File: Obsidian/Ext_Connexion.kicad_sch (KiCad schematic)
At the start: 35 parts, among them J4 Conn_02x20_Odd_Even

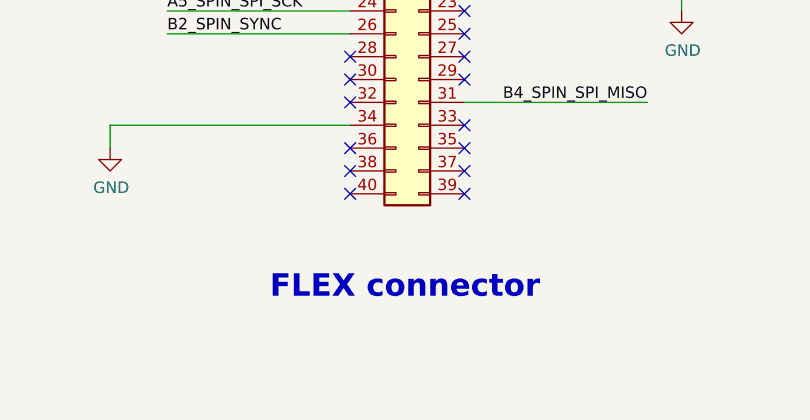
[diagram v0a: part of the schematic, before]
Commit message: Changed the layout so that we have guard rails. Changed USB and RJ45 position Changed Flex connector position. Changed flash LDO position Improved silkscreen. Changed outline around RJ45. Changed SFP cage footprint. Added a rule for Earth clearance.
Signed-off-by: Jean Alinei <jean.alinei@owntech.org>
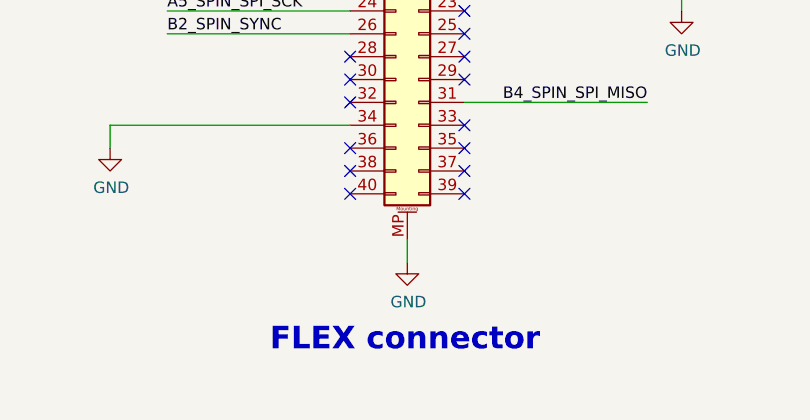
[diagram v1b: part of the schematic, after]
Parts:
- J4: symbol Connector_Generic:Conn_02x20_Odd_Even -> Connector_Generic_MountingPin:Conn_02x20_Odd_Even_MountingPin
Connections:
- net GND: now also J4.MP (MountPin)
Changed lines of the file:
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@@
 	(text "FLEX connector\n"
 		(exclude_from_sim no)
-		(at 64.516 184.404 0)
+		(at 64.516 190.246 0)
 		(effects
 			(font
@@
 	(wire
 		(pts
+			(xy 64.77 179.07) (xy 64.77 181.61)
+		)
+		(stroke
+			(width 0)
+			(type default)
+		)
+	)
+	(wire
+		(pts
 			(xy 101.6 72.39) (xy 101.6 71.12)
 		)
@@
 	)
 	(symbol
+		(lib_id "Library_Symbol:GND")
+		(at 64.77 181.61 0)
+		(unit 1)
+		(exclude_from_sim no)
+		(in_bom yes)
+		(on_board yes)
+		(dnp no)
+		(property "Reference" "#PWR0295"
+			(at 64.77 187.96 0)
+			(effects
+				(font
+					(size 1.27 1.27)
+				)
+				(hide yes)
+			)
+		)
+		(property "Value" "GND"
+			(at 64.897 186.0042 0)
+			(effects
+				(font
+					(size 1.27 1.27)
+				)
+			)
+		)
+		(property "Footprint" ""
+			(at 64.77 181.61 0)
+			(effects
+				(font
+					(size 1.27 1.27)
+				)
+				(hide yes)
+			)
+		)
+		(property "Datasheet" ""
+			(at 64.77 181.61 0)
+			(effects
+				(font
+					(size 1.27 1.27)
+				)
+				(hide yes)
+			)
+		)
+		(property "Description" ""
+			(at 64.77 181.61 0)
+			(effects
+				(font
+					(size 1.27 1.27)
+				)
+				(hide yes)
+			)
+		)
+		(pin "1"
+		)
+		(instances
+			(project "Obsidian"
+				(path "/c2a4f786-b14c-434a-acf7-b20fb2221b0b/37c76a7d-e360-409e-9f8e-819f870af943"
+					(reference "#PWR0295")
+					(unit 1)
+				)
+			)
+		)
+	)
+	(symbol
 		(lib_id "Library_Symbol:+1V0")
 		(at 191.77 44.45 0)
@@
 	)
 	(symbol
-		(lib_id "Connector_Generic:Conn_02x20_Odd_Even")
+		(lib_id "Connector_Generic_MountingPin:Conn_02x20_Odd_Even_MountingPin")
 		(at 66.04 148.59 0)
 		(mirror y)
@@
 			)
 		)
-		(property "Datasheet" "${KIPRJMOD}/datasheet/C2763968.pdf"
+		(property "Datasheet" "~"
 			(at 66.04 148.59 0)
 			(effects
@@
 			)
 		)
-		(property "Description" "Generic connector, double row, 02x20, odd/even pin numbering scheme (row 1 odd numbers, row 2 even numbers), script generated (kicad-library-utils/schlib/autogen/connector/)"
+		(property "Description" "Generic connectable mounting pin connector, double row, 02x20, odd/even pin numbering scheme (row 1 odd numbers, row 2 even numbers), script generated (kicad-library-utils/schlib/autogen/connector/)"
 			(at 66.04 148.59 0)
 			(effects
@@
 		(pin "22"
 		)
+		(pin "MP"
+		)
 		(instances

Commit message: Update schematic for out of stock components
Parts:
- R126, R128, R132, R136: LCSC C11702 -> C144789
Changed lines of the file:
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@@
 			)
 		)
-		(property "Datasheet" "${KIPRJMOD}/datasheet/C11702.pdf"
+		(property "Datasheet" "${KIPRJMOD}/datasheet/C144789.pdf"
 			(at 228.727 76.2 0)
 			(effects
@@
 			)
 		)
-		(property "LCSC" "C11702"
+		(property "LCSC" "C144789"
 			(at 237.49 76.2 0)
 			(effects
@@
 			)
 		)
-		(property "Datasheet" "${KIPRJMOD}/datasheet/C11702.pdf"
+		(property "Datasheet" "${KIPRJMOD}/datasheet/C144789.pdf"
 			(at 228.727 44.45 0)
 			(effects
@@
 			)
 		)
-		(property "LCSC" "C11702"
+		(property "LCSC" "C144789"
 			(at 237.49 44.45 0)
 			(effects
@@
 			)
 		)
-		(property "Datasheet" "${KIPRJMOD}/datasheet/C11702.pdf"
+		(property "Datasheet" "${KIPRJMOD}/datasheet/C144789.pdf"
 			(at 228.727 24.13 0)
 			(effects
@@
 			)
 		)
-		(property "LCSC" "C11702"
+		(property "LCSC" "C144789"
 			(at 237.49 24.13 0)
 			(effects
@@
 			)
 		)
-		(property "Datasheet" "${KIPRJMOD}/datasheet/C11702.pdf"
+		(property "Datasheet" "${KIPRJMOD}/datasheet/C144789.pdf"
 			(at 228.727 60.96 0)
 			(effects
@@
 			)
 		)
-		(property "LCSC" "C11702"
+		(property "LCSC" "C144789"
 			(at 237.49 60.96 0)
 			(effects
